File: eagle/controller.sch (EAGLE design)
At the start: 20 parts, among them J1 629722000214

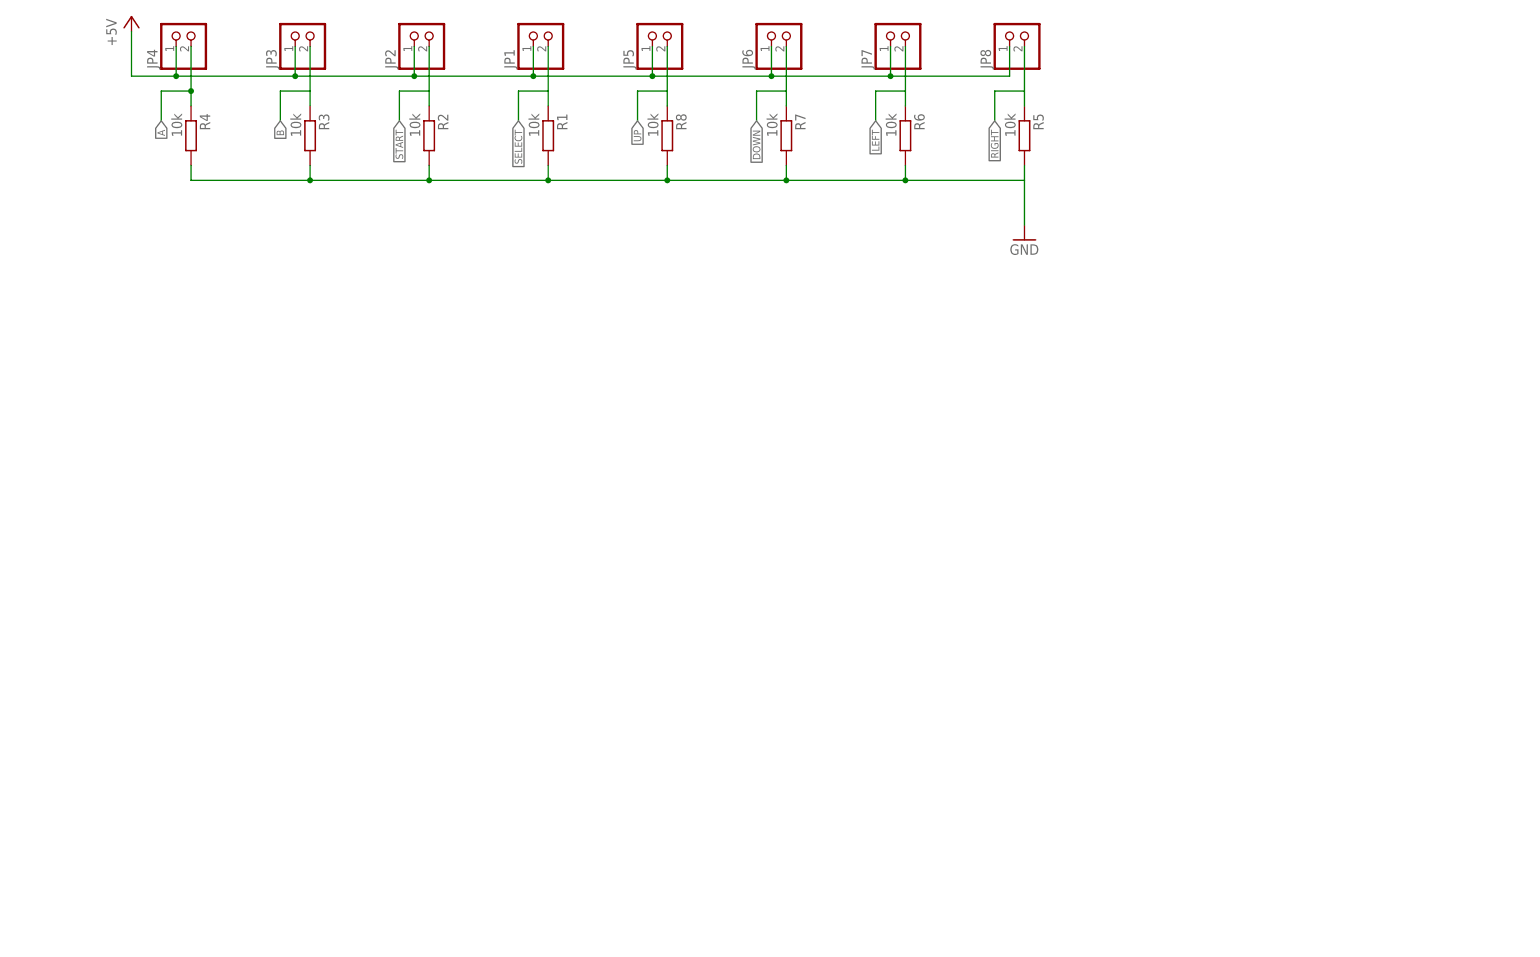
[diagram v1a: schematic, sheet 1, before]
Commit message: new controller logic implemented
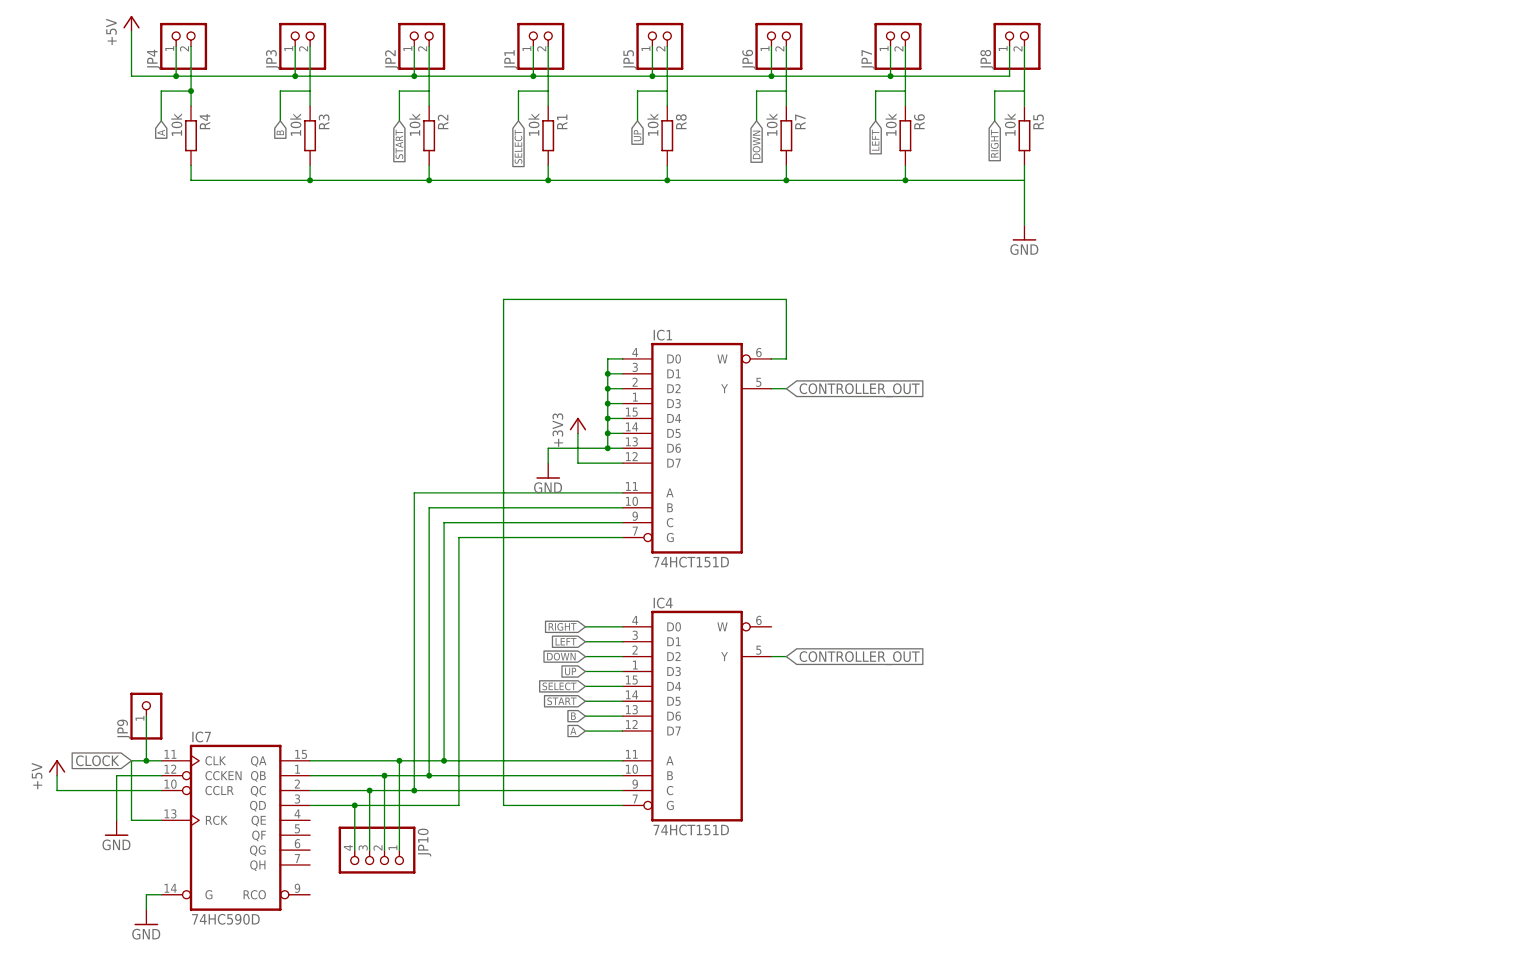
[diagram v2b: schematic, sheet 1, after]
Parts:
- removed J1: 629722000214, Eagle_WR-USB (rev22c):629722000214
- added IC1, IC4: 74HCT151D, 74xx-eu:74HCT151D
- added IC7: 74HC590D, 74xx-eu:74HC590D
- added J4: 632723100011_USBC_3.1, Eagle_WR-USB (rev22c):632723100011_USBC_3.1
- added JP10: (no value), pinhead:PINHD-1X4
- added JP9: (no value), pinhead:PINHD-1X1
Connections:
- new net +3V3: IC1A.D7
- new net CLOCK: IC7A.CLK, IC7A.RCK, J4.SSTXN1, JP9.1
- new net CONTROLLER_OUT: IC1A.Y, IC4A.Y, J4.SSTXP1
- new net N$10: IC1A.B, IC4A.B, IC7A.QB, JP10.2
- new net N$12: IC1A.W, IC4A.G
- new net N$24: IC1A.G, IC7A.QD, JP10.4
- new net N$5: IC1A.C, IC4A.A, IC7A.QA, JP10.1
- new net N$6: IC1A.A, IC4A.C, IC7A.QC, JP10.3
- net +5V: now also IC7A.CCLR
- net A: now also IC4A.D7; no longer J1.SBU2
- net B: now also IC4A.D6; no longer J1.D-2
- net DOWN: now also IC4A.D2; no longer J1.D-1
- net GND: now also IC1A.D0, IC1A.D1, IC1A.D2, IC1A.D3, IC1A.D4, IC1A.D5, IC1A.D6, IC7A.CCKEN, IC7A.G, J4.CC, J4.DN1, J4.DP1, J4.GND, J4.GND1, J4.SBU1, J4.SHIELD, J4.SHIELD1, J4.SSRXN2, J4.SSRXP2; no longer J1.GND, J1.GND1, J1.GND2, J1.GND3, J1.SHIELD
- net LEFT: now also IC4A.D1; no longer J1.D+1
- net N$3: now also J4.VBUS, J4.VBUS1; no longer J1.VBUS, J1.VBUS1, J1.VBUS2, J1.VBUS3
- net RIGHT: now also IC4A.D0; no longer J1.CC1
- net SELECT: now also IC4A.D4; no longer J1.CC2
- net START: now also IC4A.D5; no longer J1.D+2
- net UP: now also IC4A.D3; no longer J1.SBU1
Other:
- moved on the sheet: C9, R12

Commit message: erc check
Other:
- moved on the sheet: C9, J4, R12

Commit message: fixed controller.sch
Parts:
- added IC2: 74HC04D, 74xx-eu:74HC04D
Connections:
- new net N$13: IC1A.W
- net GND: now also IC2B.I, IC2C.I, IC2D.I, IC2E.I, IC2F.I
- net N$12: now also IC2A.O; no longer IC1A.W
- net N$24: now also IC2A.I
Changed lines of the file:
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@@
 <part name="GND4" library="supply1" library_urn="urn:adsk.eagle:library:371" deviceset="GND" device=""/>
 <part name="GND5" library="supply1" library_urn="urn:adsk.eagle:library:371" deviceset="GND" device=""/>
+<part name="IC2" library="74xx-eu" library_urn="urn:adsk.eagle:library:85" deviceset="74*04" device="D" package3d_urn="urn:adsk.eagle:package:1010/2" technology="HC"/>
+<part name="GND7" library="supply1" library_urn="urn:adsk.eagle:library:371" deviceset="GND" device=""/>
+<part name="GND8" library="supply1" library_urn="urn:adsk.eagle:library:371" deviceset="GND" device=""/>
+<part name="GND9" library="supply1" library_urn="urn:adsk.eagle:library:371" deviceset="GND" device=""/>
+<part name="GND10" library="supply1" library_urn="urn:adsk.eagle:library:371" deviceset="GND" device=""/>
+<part name="GND11" library="supply1" library_urn="urn:adsk.eagle:library:371" deviceset="GND" device=""/>
 </parts>
 <sheets>
@@
 <instance part="+3V1" gate="G$1" x="99.06" y="96.52" smashed="yes">
 <attribute name="VALUE" x="96.52" y="91.44" size="1.778" layer="96" rot="R90"/>
+</instance>
+<instance part="IC2" gate="A" x="91.44" y="25.4" smashed="yes">
+<attribute name="NAME" x="93.98" y="28.575" size="1.778" layer="95"/>
+<attribute name="VALUE" x="93.98" y="20.32" size="1.778" layer="96"/>
+</instance>
+<instance part="IC2" gate="B" x="246.38" y="127" smashed="yes">
+<attribute name="NAME" x="248.92" y="130.175" size="1.778" layer="95"/>
+<attribute name="VALUE" x="248.92" y="121.92" size="1.778" layer="96"/>
+</instance>
+<instance part="IC2" gate="C" x="246.38" y="114.3" smashed="yes">
+<attribute name="NAME" x="248.92" y="117.475" size="1.778" layer="95"/>
+<attribute name="VALUE" x="248.92" y="109.22" size="1.778" layer="96"/>
+</instance>
+<instance part="IC2" gate="D" x="246.38" y="101.6" smashed="yes">
+<attribute name="NAME" x="248.92" y="104.775" size="1.778" layer="95"/>
+<attribute name="VALUE" x="248.92" y="96.52" size="1.778" layer="96"/>
+</instance>
+<instance part="IC2" gate="E" x="246.38" y="88.9" smashed="yes">
+<attribute name="NAME" x="248.92" y="92.075" size="1.778" layer="95"/>
+<attribute name="VALUE" x="248.92" y="83.82" size="1.778" layer="96"/>
+</instance>
+<instance part="IC2" gate="F" x="246.38" y="76.2" smashed="yes">
+<attribute name="NAME" x="248.92" y="79.375" size="1.778" layer="95"/>
+<attribute name="VALUE" x="248.92" y="71.12" size="1.778" layer="96"/>
+</instance>
+<instance part="GND7" gate="1" x="233.68" y="71.12" smashed="yes">
+<attribute name="VALUE" x="231.14" y="68.58" size="1.778" layer="96"/>
+</instance>
+<instance part="GND8" gate="1" x="233.68" y="83.82" smashed="yes">
+<attribute name="VALUE" x="231.14" y="81.28" size="1.778" layer="96"/>
+</instance>
+<instance part="GND9" gate="1" x="233.68" y="96.52" smashed="yes">
+<attribute name="VALUE" x="231.14" y="93.98" size="1.778" layer="96"/>
+</instance>
+<instance part="GND10" gate="1" x="233.68" y="109.22" smashed="yes">
+<attribute name="VALUE" x="231.14" y="106.68" size="1.778" layer="96"/>
+</instance>
+<instance part="GND11" gate="1" x="233.68" y="121.92" smashed="yes">
+<attribute name="VALUE" x="231.14" y="119.38" size="1.778" layer="96"/>
 </instance>
 </instances>
@@
 <junction x="104.14" y="91.44"/>
 </segment>
+<segment>
+<pinref part="IC2" gate="F" pin="I"/>
+<wire x1="236.22" y1="76.2" x2="233.68" y2="76.2" width="0.1524" layer="91"/>
+<wire x1="233.68" y1="76.2" x2="233.68" y2="73.66" width="0.1524" layer="91"/>
+<pinref part="GND7" gate="1" pin="GND"/>
+</segment>
+<segment>
+<wire x1="236.22" y1="88.9" x2="233.68" y2="88.9" width="0.1524" layer="91"/>
+<wire x1="233.68" y1="88.9" x2="233.68" y2="86.36" width="0.1524" layer="91"/>
+<pinref part="GND8" gate="1" pin="GND"/>
+<pinref part="IC2" gate="E" pin="I"/>
+</segment>
+<segment>
+<wire x1="236.22" y1="101.6" x2="233.68" y2="101.6" width="0.1524" layer="91"/>
+<wire x1="233.68" y1="101.6" x2="233.68" y2="99.06" width="0.1524" layer="91"/>
+<pinref part="GND9" gate="1" pin="GND"/>
+<pinref part="IC2" gate="D" pin="I"/>
+</segment>
+<segment>
+<wire x1="236.22" y1="114.3" x2="233.68" y2="114.3" width="0.1524" layer="91"/>
+<wire x1="233.68" y1="114.3" x2="233.68" y2="111.76" width="0.1524" layer="91"/>
+<pinref part="GND10" gate="1" pin="GND"/>
+<pinref part="IC2" gate="C" pin="I"/>
+</segment>
+<segment>
+<wire x1="236.22" y1="127" x2="233.68" y2="127" width="0.1524" layer="91"/>
+<wire x1="233.68" y1="127" x2="233.68" y2="124.46" width="0.1524" layer="91"/>
+<pinref part="GND11" gate="1" pin="GND"/>
+<pinref part="IC2" gate="B" pin="I"/>
+</segment>
 </net>
 <net name="B" class="0">
@@
 <pinref part="IC1" gate="A" pin="G"/>
 <wire x1="78.74" y1="76.2" x2="106.68" y2="76.2" width="0.1524" layer="91"/>
+<wire x1="78.74" y1="30.48" x2="78.74" y2="25.4" width="0.1524" layer="91"/>
+<junction x="78.74" y="30.48"/>
+<pinref part="IC2" gate="A" pin="I"/>
+<wire x1="78.74" y1="25.4" x2="81.28" y2="25.4" width="0.1524" layer="91"/>
 </segment>
 </net>
@@
 </segment>
 </net>
-<net name="N$12" class="0">
-<segment>
-<pinref part="IC1" gate="A" pin="W"/>
-<wire x1="132.08" y1="106.68" x2="134.62" y2="106.68" width="0.1524" layer="91"/>
-<wire x1="134.62" y1="106.68" x2="134.62" y2="116.84" width="0.1524" layer="91"/>
-<wire x1="134.62" y1="116.84" x2="86.36" y2="116.84" width="0.1524" layer="91"/>
-<wire x1="86.36" y1="116.84" x2="86.36" y2="30.48" width="0.1524" layer="91"/>
-<pinref part="IC4" gate="A" pin="G"/>
-<wire x1="86.36" y1="30.48" x2="106.68" y2="30.48" width="0.1524" layer="91"/>
-</segment>
-</net>
 <net name="CONTROLLER_OUT" class="0">
 <segment>
@@
 </segment>
 </net>
+<net name="N$13" class="0">
+<segment>
+<pinref part="IC1" gate="A" pin="W"/>
+<wire x1="132.08" y1="106.68" x2="134.62" y2="106.68" width="0.1524" layer="91"/>
+</segment>
+</net>
+<net name="N$12" class="0">
+<segment>
+<pinref part="IC2" gate="A" pin="O"/>
+<wire x1="101.6" y1="25.4" x2="104.14" y2="25.4" width="0.1524" layer="91"/>
+<wire x1="104.14" y1="25.4" x2="104.14" y2="30.48" width="0.1524" layer="91"/>
+<pinref part="IC4" gate="A" pin="G"/>
+<wire x1="104.14" y1="30.48" x2="106.68" y2="30.48" width="0.1524" layer="91"/>
+</segment>
+</net>

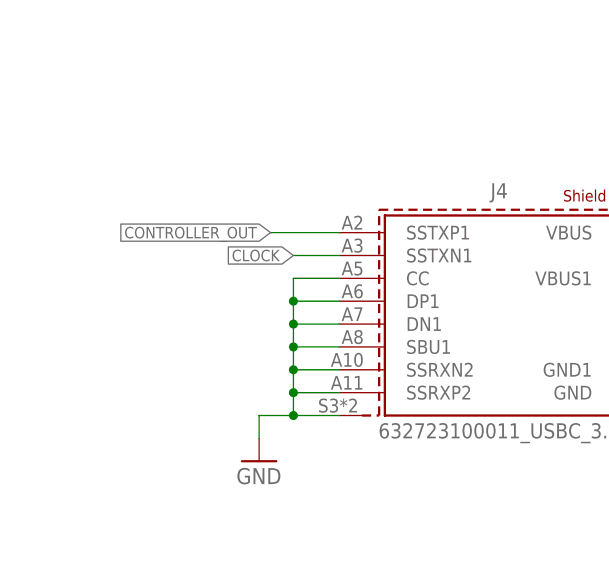
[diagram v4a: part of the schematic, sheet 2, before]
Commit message: changed usb-c pin used by controller
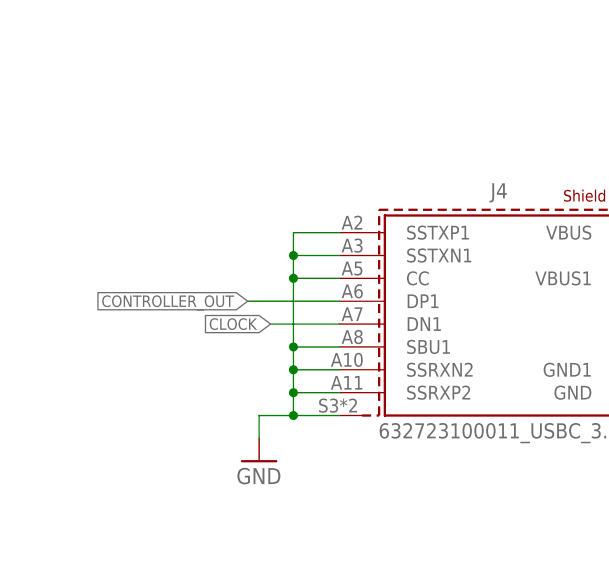
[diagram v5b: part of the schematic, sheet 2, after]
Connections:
- net CLOCK: now also J4.DN1; no longer J4.SSTXN1
- net CONTROLLER_OUT: now also J4.DP1; no longer J4.SSTXP1
- net GND: now also J4.SSTXN1, J4.SSTXP1; no longer J4.DN1, J4.DP1
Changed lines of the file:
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@@
 <wire x1="50.8" y1="40.64" x2="50.8" y2="43.18" width="0.1524" layer="91"/>
 <wire x1="50.8" y1="43.18" x2="50.8" y2="45.72" width="0.1524" layer="91"/>
-<wire x1="50.8" y1="45.72" x2="50.8" y2="48.26" width="0.1524" layer="91"/>
-<wire x1="50.8" y1="48.26" x2="50.8" y2="50.8" width="0.1524" layer="91"/>
-<wire x1="50.8" y1="50.8" x2="50.8" y2="53.34" width="0.1524" layer="91"/>
-<wire x1="50.8" y1="53.34" x2="55.88" y2="53.34" width="0.1524" layer="91"/>
-<wire x1="50.8" y1="50.8" x2="55.88" y2="50.8" width="0.1524" layer="91"/>
-<junction x="50.8" y="50.8"/>
-<wire x1="50.8" y1="48.26" x2="55.88" y2="48.26" width="0.1524" layer="91"/>
-<junction x="50.8" y="48.26"/>
 <wire x1="55.88" y1="45.72" x2="50.8" y2="45.72" width="0.1524" layer="91"/>
-<junction x="50.8" y="45.72"/>
 <wire x1="50.8" y1="43.18" x2="55.88" y2="43.18" width="0.1524" layer="91"/>
 <junction x="50.8" y="43.18"/>
-<pinref part="J4" gate="G$1" pin="CC"/>
-<pinref part="J4" gate="G$1" pin="DP1"/>
-<pinref part="J4" gate="G$1" pin="DN1"/>
 <pinref part="J4" gate="G$1" pin="SBU1"/>
 <pinref part="J4" gate="G$1" pin="SSRXN2"/>
@@
 <wire x1="46.99" y1="38.1" x2="50.8" y2="38.1" width="0.1524" layer="91"/>
 <junction x="50.8" y="38.1"/>
+<wire x1="50.8" y1="45.72" x2="50.8" y2="53.34" width="0.1524" layer="91"/>
+<junction x="50.8" y="45.72"/>
+<pinref part="J4" gate="G$1" pin="SSTXP1"/>
+<wire x1="50.8" y1="53.34" x2="50.8" y2="55.88" width="0.1524" layer="91"/>
+<wire x1="50.8" y1="55.88" x2="50.8" y2="58.42" width="0.1524" layer="91"/>
+<wire x1="50.8" y1="58.42" x2="55.88" y2="58.42" width="0.1524" layer="91"/>
+<pinref part="J4" gate="G$1" pin="SSTXN1"/>
+<wire x1="55.88" y1="55.88" x2="50.8" y2="55.88" width="0.1524" layer="91"/>
+<junction x="50.8" y="55.88"/>
+<pinref part="J4" gate="G$1" pin="CC"/>
+<wire x1="55.88" y1="53.34" x2="50.8" y2="53.34" width="0.1524" layer="91"/>
+<junction x="50.8" y="53.34"/>
 </segment>
 <segment>
@@
 <net name="CONTROLLER_OUT" class="0">
 <segment>
-<wire x1="55.88" y1="58.42" x2="48.26" y2="58.42" width="0.1524" layer="91"/>
-<label x="48.26" y="58.42" size="1.27" layer="95" rot="R180" xref="yes"/>
-<pinref part="J4" gate="G$1" pin="SSTXP1"/>
+<wire x1="55.88" y1="50.8" x2="45.72" y2="50.8" width="0.1524" layer="91"/>
+<label x="45.72" y="50.8" size="1.27" layer="95" rot="R180" xref="yes"/>
+<pinref part="J4" gate="G$1" pin="DP1"/>
 </segment>
 </net>
 <net name="CLOCK" class="0">
 <segment>
-<pinref part="J4" gate="G$1" pin="SSTXN1"/>
-<wire x1="55.88" y1="55.88" x2="50.8" y2="55.88" width="0.1524" layer="91"/>
-<label x="50.8" y="55.88" size="1.27" layer="95" rot="R180" xref="yes"/>
+<wire x1="55.88" y1="48.26" x2="48.26" y2="48.26" width="0.1524" layer="91"/>
+<label x="48.26" y="48.26" size="1.27" layer="95" rot="R180" xref="yes"/>
+<pinref part="J4" gate="G$1" pin="DN1"/>
 </segment>
 </net>

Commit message: finalized schematik with detommaso and spiss supervision
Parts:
- removed C1: 100nF, rcl:C-EUC0805
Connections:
- removed net +3.3V: C1.1
- net GND: no longer C1.2
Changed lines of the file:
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@@
 <part name="FRAME1" library="frames" library_urn="urn:adsk.eagle:library:229" deviceset="DINA4_L" device=""/>
 <part name="FRAME2" library="frames" library_urn="urn:adsk.eagle:library:229" deviceset="DINA4_L" device=""/>
-<part name="GND2" library="supply1" library_urn="urn:adsk.eagle:library:371" deviceset="GND" device=""/>
-<part name="C1" library="rcl" library_urn="urn:adsk.eagle:library:334" deviceset="C-EU" device="C0805" package3d_urn="urn:adsk.eagle:package:23617/2" value="100nF"/>
-<part name="P+1" library="supply1" library_urn="urn:adsk.eagle:library:371" deviceset="+5V" device=""/>
 <part name="JP1" library="pinhead" library_urn="urn:adsk.eagle:library:325" deviceset="PINHD-1X2" device="" package3d_urn="urn:adsk.eagle:package:22435/2"/>
 <part name="JP2" library="pinhead" library_urn="urn:adsk.eagle:library:325" deviceset="PINHD-1X2" device="" package3d_urn="urn:adsk.eagle:package:22435/2"/>
@@
 <attribute name="DRAWING_NAME" x="180.34" y="19.05" size="2.54" layer="94"/>
 </instance>
-<instance part="GND2" gate="1" x="25.4" y="138.43" smashed="yes">
-<attribute name="VALUE" x="22.86" y="135.89" size="1.778" layer="96"/>
-</instance>
-<instance part="C1" gate="G$1" x="25.4" y="152.4" smashed="yes">
-<attribute name="NAME" x="26.924" y="152.781" size="1.778" layer="95"/>
-<attribute name="VALUE" x="26.924" y="147.701" size="1.778" layer="96"/>
-</instance>
-<instance part="P+1" gate="1" x="25.4" y="163.83" smashed="yes">
-<attribute name="VALUE" x="22.86" y="158.75" size="1.778" layer="96" rot="R90"/>
-</instance>
 <instance part="R12" gate="G$1" x="102.87" y="55.88" smashed="yes">
 <attribute name="NAME" x="105.41" y="56.1975" size="0.8128" layer="95"/>
@@
 <nets>
 <net name="GND" class="0">
-<segment>
-<pinref part="GND2" gate="1" pin="GND"/>
-<pinref part="C1" gate="G$1" pin="2"/>
-<wire x1="25.4" y1="147.32" x2="25.4" y2="140.97" width="0.1524" layer="91"/>
-</segment>
 <segment>
 <pinref part="C9" gate="G$1" pin="1"/>
@@
 </segment>
 </net>
-<net name="+3.3V" class="0">
-<segment>
-<pinref part="C1" gate="G$1" pin="1"/>
-<wire x1="25.4" y1="154.94" x2="25.4" y2="161.29" width="0.1524" layer="91"/>
-<pinref part="P+1" gate="1" pin="+5V"/>
-</segment>
-</net>
 <net name="N$3" class="0">
 <segment>
@@
 packages will not be understood (or retained) with this version.
 </note>
-<note version="8.4" severity="warning">
-Since Version 8.4, EAGLE supports properties for SPICE simulation.
-Probes in schematics and SPICE mapping objects found in parts and library devices
-will not be understood with this version. Update EAGLE to the latest version
-for full support of SPICE simulation.
-</note>
 </compatibility>
